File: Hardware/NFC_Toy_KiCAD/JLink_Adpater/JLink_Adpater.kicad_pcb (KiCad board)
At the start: 2 copper layers, 13.8 x 14.7 mm, 2 parts, among them J1 JLink_Mini, J2 JLink_Mini

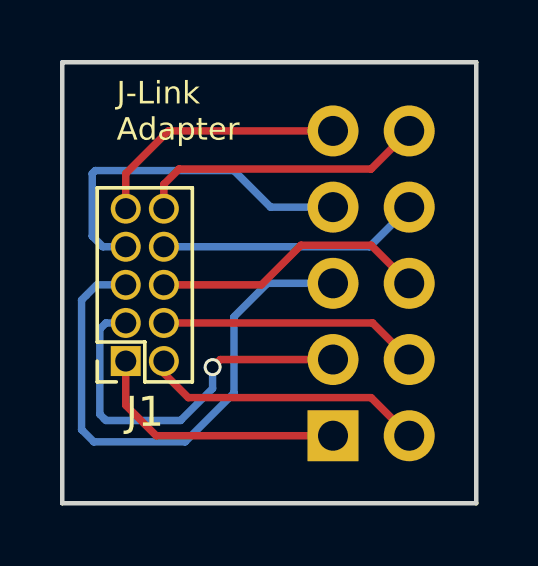
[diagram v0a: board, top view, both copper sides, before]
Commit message: Added inverted JLink adapter. First working code.
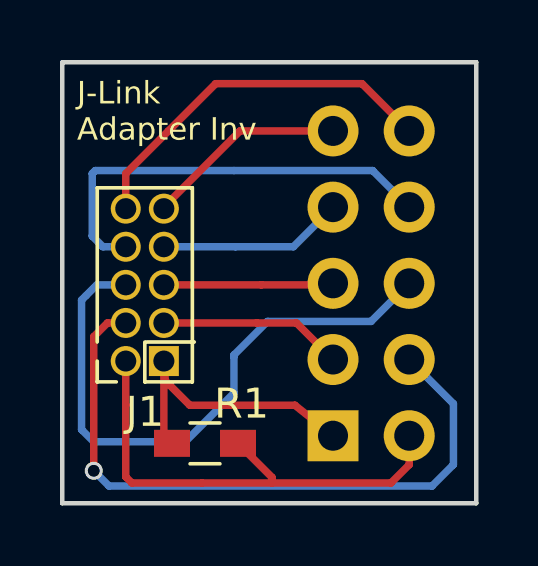
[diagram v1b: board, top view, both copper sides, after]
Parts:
- added R1: 100k, Resistors_SMD:R_0603_HandSoldering, F.Cu at (149.8, 114.5)
- J1: footprint Socket_Strips:Socket_Strip_Straight_2x05_Pitch1.27mm -> NFC_Toy_Lib:JLink_Mini_0p05_inverted
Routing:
- net Net-(J1-Pad4): track 8.68 -> 22.3 mm, vias 0 -> 1
- net Net-(J1-Pad5): track 18.2 -> 5.66 mm
- net Net-(J1-Pad6): track 9.25 -> 20.0 mm
- net Net-(J1-Pad2): track 9.45 -> 16.4 mm
- net Net-(J1-Pad3): track 12.9 -> 6.14 mm, vias 1 -> 0
- net Net-(J1-Pad8): track 8.73 -> 14.5 mm
- net Net-(J1-Pad7): track 11.9 -> 6.19 mm
- net Net-(J1-Pad10): track 9.73 -> 12.5 mm
- net Net-(J1-Pad9): track 8.67 -> 6.74 mm
- net Net-(J1-Pad1): track 8.80 -> 9.80 mm
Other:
- board text added: "J-Link Adapter Inv"
- board text removed: "J-Link Adapter"
